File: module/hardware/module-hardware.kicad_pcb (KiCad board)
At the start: 4 copper layers, 45.7 x 125.7 mm, 87 parts, among them J1 USB_B_Micro, J10 Conn_01x03, J11 Conn_01x03, J12 Conn_01x03, J13 0, J2 40Pin 0.1", J3 Conn_01x02_Male, J4 40Pin 0.1", J5 Conn_01x03_Male, J6 Conn_01x03_Male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

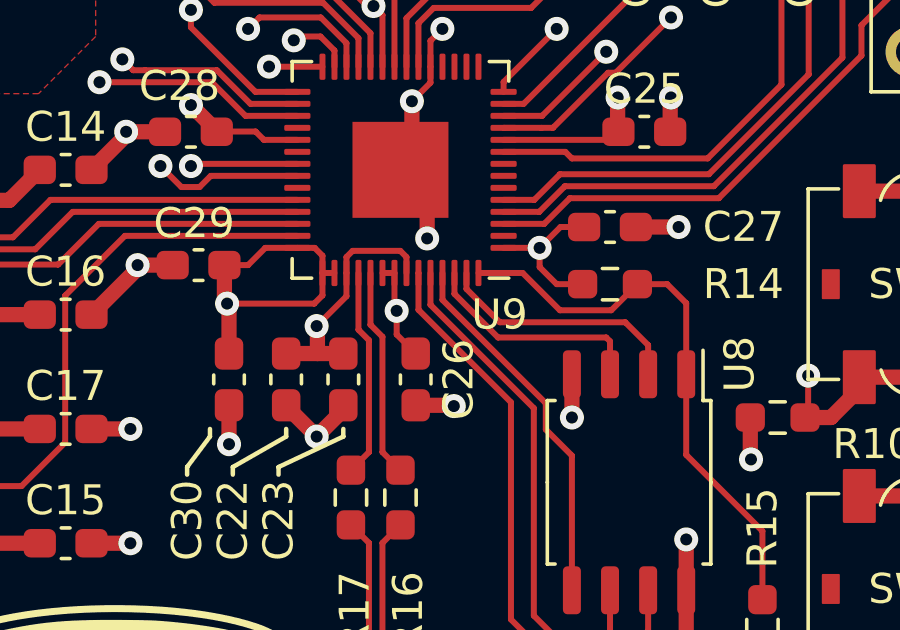
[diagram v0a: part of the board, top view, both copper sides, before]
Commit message: Add project copy of RP2040 footprint
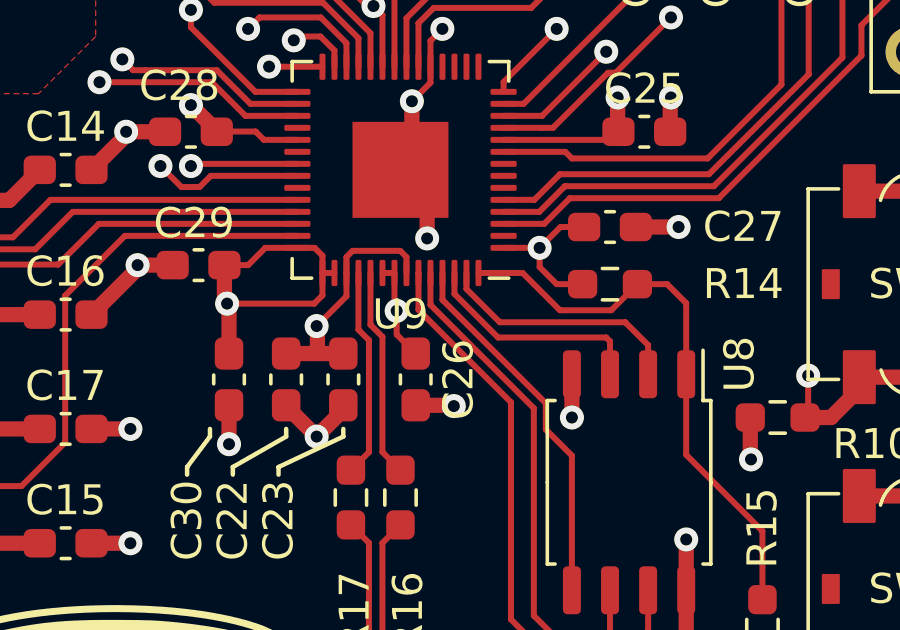
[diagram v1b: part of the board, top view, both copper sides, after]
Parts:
- U9: footprint Package_DFN_QFN:QFN-56-1EP_7x7mm_P0.4mm_EP3.2x3.2mm -> DRUM Library:QFN-56-1EP_7x7mm_P0.4mm_EP3.2x3.2mm
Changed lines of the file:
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@@
     )
   )
-  (footprint "Package_DFN_QFN:QFN-56-1EP_7x7mm_P0.4mm_EP3.2x3.2mm" (layer "F.Cu")
+  (footprint "DRUM Library:QFN-56-1EP_7x7mm_P0.4mm_EP3.2x3.2mm" (layer "F.Cu")
     (at 150.495 129.54 180)
     (descr "QFN, 56 Pin (https://datasheets.raspberrypi.com/rp2040/rp2040-datasheet.pdf#page=634), generated with kicad-footprint-generator ipc_noLead_generator.py")
@@
     (property "Sheetname" "D.R.U.M. Module Digital")
     (attr smd)
-    (fp_text reference "U9" (at -3.302 -4.826) (layer "F.SilkS")
+    (fp_text reference "U9" (at 0 -4.82 180) (layer "F.SilkS")
       (effects (font (size 1 1) (thickness 0.15)))
     )
-    (fp_text value "RP2040" (at 0 4.82) (layer "F.Fab")
+    (fp_text value "RP2040" (at 0 4.82 180) (layer "F.Fab")
       (effects (font (size 1 1) (thickness 0.15)))
     )
-    (fp_text user "${REFERENCE}" (at 0 0) (layer "F.Fab")
+    (fp_text user "${REFERENCE}" (at 0 0 180) (layer "F.Fab")
       (effects (font (size 1 1) (thickness 0.15)))
     )
+    (fp_line (start 3.61 -3.61) (end 3.61 -2.96) (layer "F.SilkS") (width 0.12))
+    (fp_line (start 2.96 3.61) (end 3.61 3.61) (layer "F.SilkS") (width 0.12))
+    (fp_line (start 2.96 -3.61) (end 3.61 -3.61) (layer "F.SilkS") (width 0.12))
+    (fp_line (start -2.96 3.61) (end -3.61 3.61) (layer "F.SilkS") (width 0.12))
     (fp_line (start -2.96 -3.61) (end -3.61 -3.61) (layer "F.SilkS") (width 0.12))
-    (fp_line (start 2.96 -3.61) (end 3.61 -3.61) (layer "F.SilkS") (width 0.12))
-    (fp_line (start 2.96 3.61) (end 3.61 3.61) (layer "F.SilkS") (width 0.12))
     (fp_line (start 3.61 3.61) (end 3.61 2.96) (layer "F.SilkS") (width 0.12))
     (fp_line (start -3.61 3.61) (end -3.61 2.96) (layer "F.SilkS") (width 0.12))
-    (fp_line (start -2.96 3.61) (end -3.61 3.61) (layer "F.SilkS") (width 0.12))
-    (fp_line (start 3.61 -3.61) (end 3.61 -2.96) (layer "F.SilkS") (width 0.12))
+    (fp_line (start 4.12 4.12) (end 4.12 -4.12) (layer "F.CrtYd") (width 0.05))
     (fp_line (start -4.12 -4.12) (end -4.12 4.12) (layer "F.CrtYd") (width 0.05))
     (fp_line (start 4.12 -4.12) (end -4.12 -4.12) (layer "F.CrtYd") (width 0.05))
-    (fp_line (start 4.12 4.12) (end 4.12 -4.12) (layer "F.CrtYd") (width 0.05))
     (fp_line (start -4.12 4.12) (end 4.12 4.12) (layer "F.CrtYd") (width 0.05))
+    (fp_line (start 3.5 3.5) (end -3.5 3.5) (layer "F.Fab") (width 0.1))
+    (fp_line (start 3.5 -3.5) (end 3.5 3.5) (layer "F.Fab") (width 0.1))
+    (fp_line (start -3.5 3.5) (end -3.5 -2.5) (layer "F.Fab") (width 0.1))
+    (fp_line (start -3.5 -2.5) (end -2.5 -3.5) (layer "F.Fab") (width 0.1))
     (fp_line (start -2.5 -3.5) (end 3.5 -3.5) (layer "F.Fab") (width 0.1))
-    (fp_line (start 3.5 -3.5) (end 3.5 3.5) (layer "F.Fab") (width 0.1))
-    (fp_line (start 3.5 3.5) (end -3.5 3.5) (layer "F.Fab") (width 0.1))
-    (fp_line (start -3.5 -2.5) (end -2.5 -3.5) (layer "F.Fab") (width 0.1))
-    (fp_line (start -3.5 3.5) (end -3.5 -2.5) (layer "F.Fab") (width 0.1))
+    (pad "" smd roundrect locked (at -0.8 0.8 180) (size 1.29 1.29) (layers "F.Paste") (roundrect_rratio 0.193798))
     (pad "" smd roundrect locked (at -0.8 -0.8 180) (size 1.29 1.29) (layers "F.Paste") (roundrect_rratio 0.193798))
     (pad "" smd roundrect locked (at 0.8 0.8 180) (size 1.29 1.29) (layers "F.Paste") (roundrect_rratio 0.193798))
-    (pad "" smd roundrect locked (at -0.8 0.8 180) (size 1.29 1.29) (layers "F.Paste") (roundrect_rratio 0.193798))
     (pad "" smd roundrect locked (at 0.8 -0.8 180) (size 1.29 1.29) (layers "F.Paste") (roundrect_rratio 0.193798))
     (pad "1" smd roundrect locked (at -3.4375 -2.6 180) (size 0.875 0.2) (layers "F.Cu" "F.Paste" "F.Mask") (roundrect_rratio 0.25)

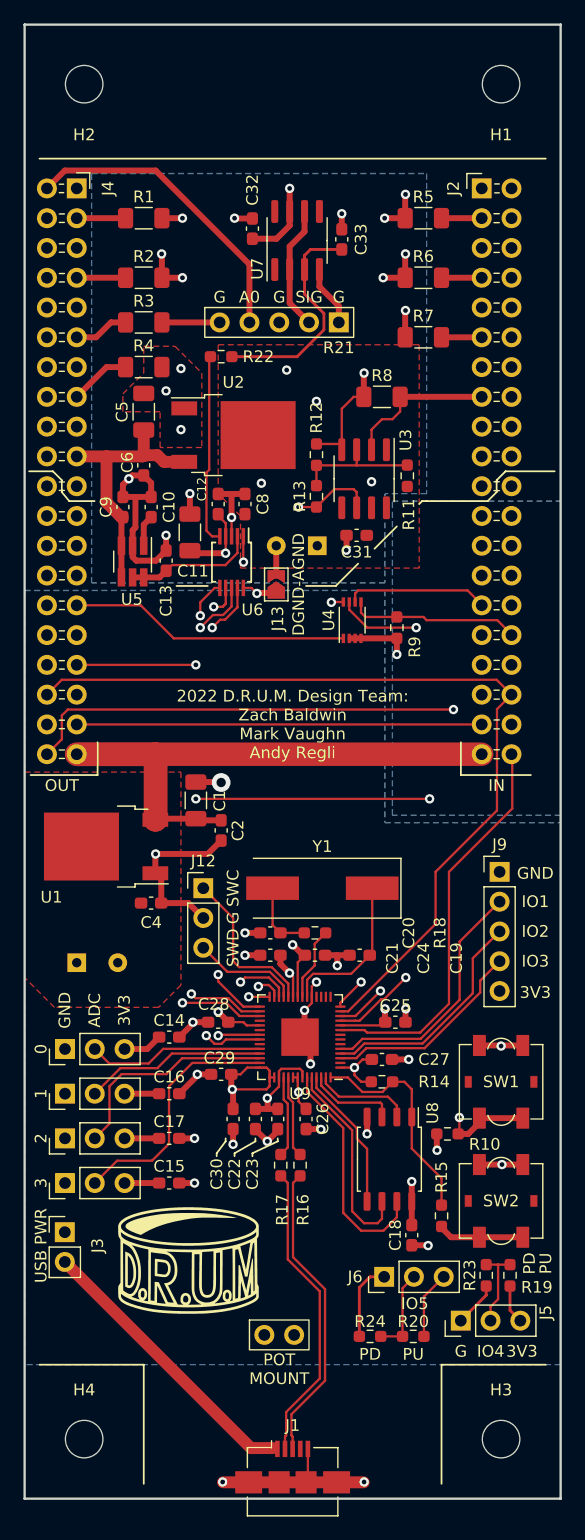
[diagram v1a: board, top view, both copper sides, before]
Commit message: Add test points; update silkscreen
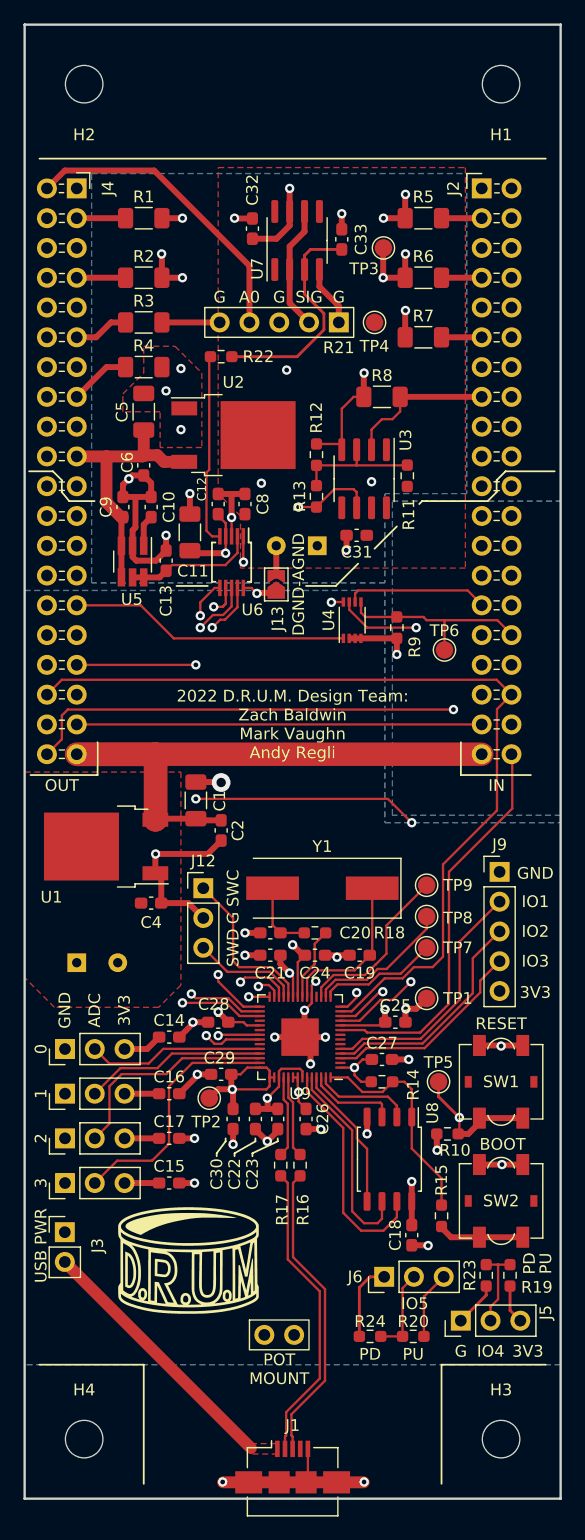
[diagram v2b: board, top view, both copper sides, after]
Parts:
- added TP1: TestPoint, TestPoint:TestPoint_Pad_D1.5mm, F.Cu at (161.3, 126.2)
- added TP2: TestPoint, TestPoint:TestPoint_Pad_D1.5mm, F.Cu at (142.7, 134.7)
- added TP3: TestPoint, TestPoint:TestPoint_Pad_D1.5mm, F.Cu at (157.6, 62.2)
- added TP4: TestPoint, TestPoint:TestPoint_Pad_D1.5mm, F.Cu at (156.8, 68.6)
- added TP5: TestPoint, TestPoint:TestPoint_Pad_D1.5mm, F.Cu at (162.3, 133.3)
- added TP6: TestPoint, TestPoint:TestPoint_Pad_D1.5mm, F.Cu at (162.8, 96.5)
- added TP7: TestPoint, TestPoint:TestPoint_Pad_D1.5mm, F.Cu at (161.3, 121.9)
- added TP8: TestPoint, TestPoint:TestPoint_Pad_D1.5mm, F.Cu at (161.3, 119.3)
- added TP9: TestPoint, TestPoint:TestPoint_Pad_D1.5mm, F.Cu at (161.3, 116.6)
- U9: footprint DRUM Library:QFN-56-1EP_7x7mm_P0.4mm_EP3.2x3.2mm -> Package_DFN_QFN:QFN-56-1EP_7x7mm_P0.4mm_EP3.2x3.2mm
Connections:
- U9 pad 15: unconnected-(U9-Pad15) -> Net-(U9-Pad15)
- U9 pad 16: unconnected-(U9-Pad16) -> Net-(U9-Pad16)
- U9 pad 17: unconnected-(U9-Pad17) -> Net-(U9-Pad17)
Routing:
- net Net-(U9-Pad17): track 0.00 -> 14.8 mm
- net Net-(U9-Pad16): track 0.00 -> 12.4 mm
- net Net-(U9-Pad15): track 0.00 -> 10.2 mm
- net GND: track 98.6 -> 104.4 mm, vias 25 -> 27
- net /RUN: track 84.9 -> 88.7 mm
- net /CBUS_SDIN: track 64.7 -> 61.8 mm
- net GNDA: track 75.2 -> 77.8 mm
- net /CBUS_NEXTPRSNT: track 14.6 -> 17.1 mm
- net +3V3: track 62.4 -> 64.6 mm
- net /CBUS_SCK: track 74.1 -> 76.1 mm
- net Net-(J1-Pad1): track 24.4 -> 22.5 mm
- net +3.3VA: vias 6 -> 5
- added copper zone on F.Cu, net Net-(J1-Pad1)
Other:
- board text added: "BOOT"
- board text added: "RESET"

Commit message: Export Gerbers
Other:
- rule pad_to_mask_clearance: 0.05 -> 0
